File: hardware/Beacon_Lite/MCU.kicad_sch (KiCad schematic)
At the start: 11 parts, among them J2 0402, SW1 SW_Push, SW2 SW_Push, U1 ESP32-S3FH4R2

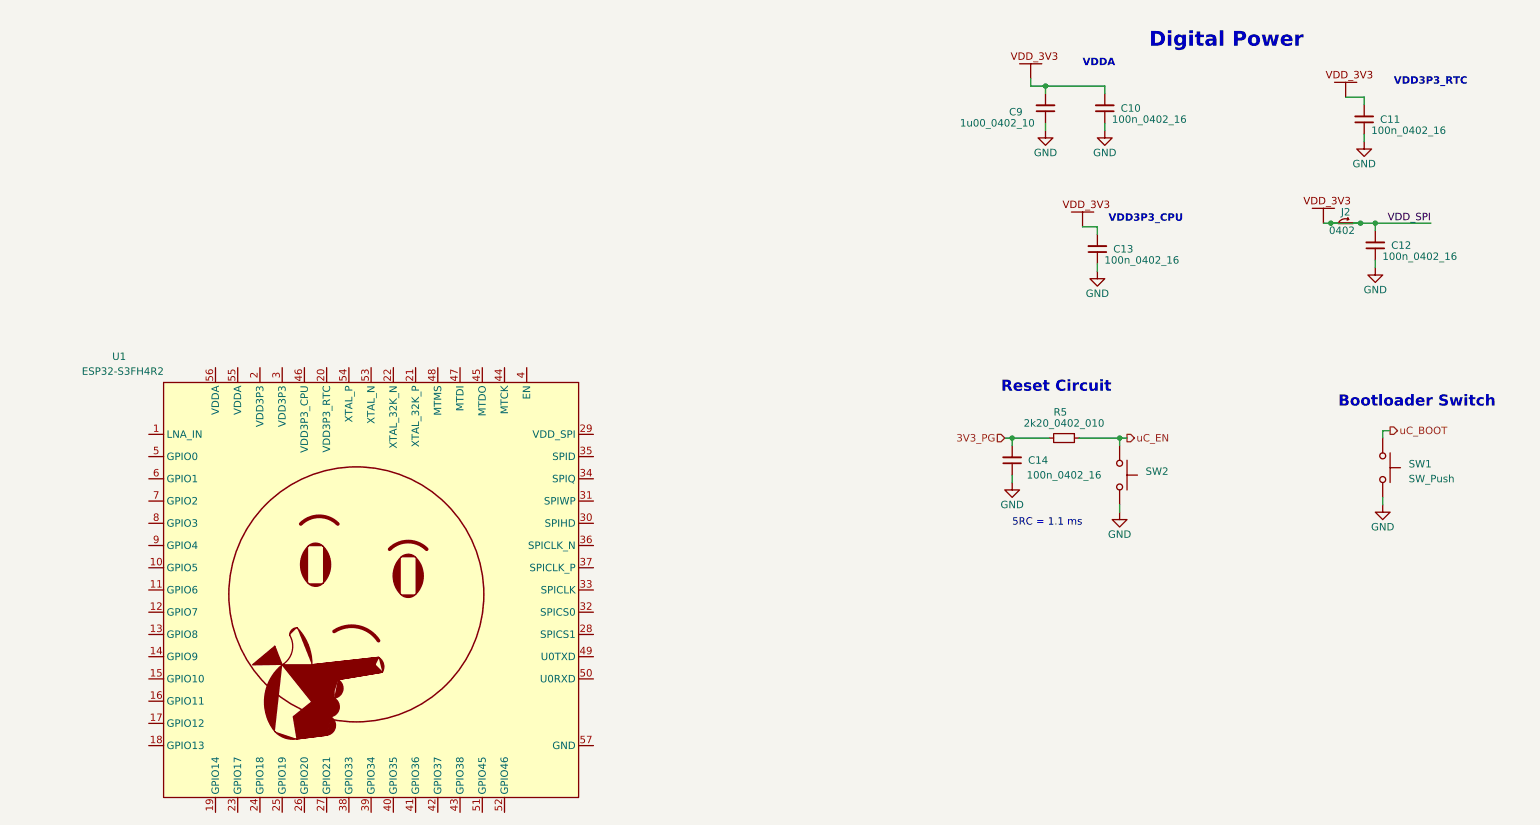
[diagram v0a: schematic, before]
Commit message: Started ST project. Create sch symbols.
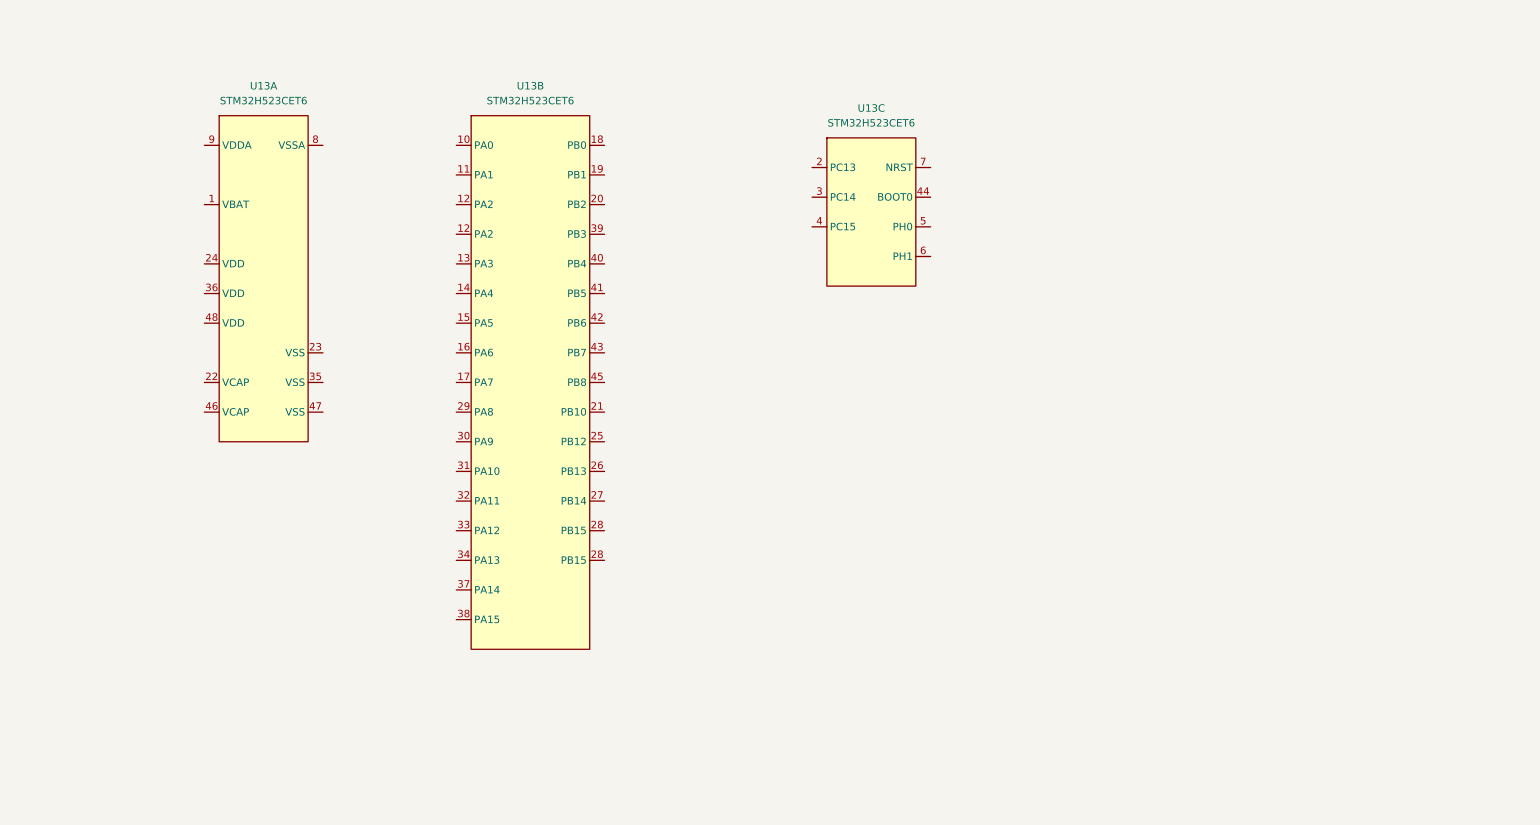
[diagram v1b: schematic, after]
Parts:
- removed C10, C11, C12, C13, C14: 100n_0402_16, Footprint_Library:0402_1005Metric_Handsolder, symbol Device:C_Small
- removed C9: 1u00_0402_10, Footprint_Library:0402_1005Metric_Handsolder, symbol Device:C_Small
- removed J2: 0402, Footprint_Library:0402_CUT-N-JUMP, symbol Beacon_Library:CUT_N_JUMP
- removed R5: 2k20_0402_010, Footprint_Library:0402_1005Metric_Handsolder, symbol Device:R_Small
- removed SW1, SW2: SW_Push, Footprint_Library:SW_PUSH_6mm, symbol Switch:SW_Push
- removed U1: ESP32-S3FH4R2, Footprint_Library:QFN40P700X700X90-57N-D, symbol Beacon_Library:ESP32-S3FH4R2
- added U13: STM32H523CET6, symbol Beacon_Lite_Library:STM32H523CET6
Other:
- note removed: "5RC = 1.1 ms"
- note removed: "Bootloader Switch"
- note removed: "Digital Power"
- note removed: "Reset Circuit"
- note removed: "VDD3P3_CPU"
- note removed: "VDD3P3_RTC"
- note removed: "VDDA"

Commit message: Minor schematic and symbol updates
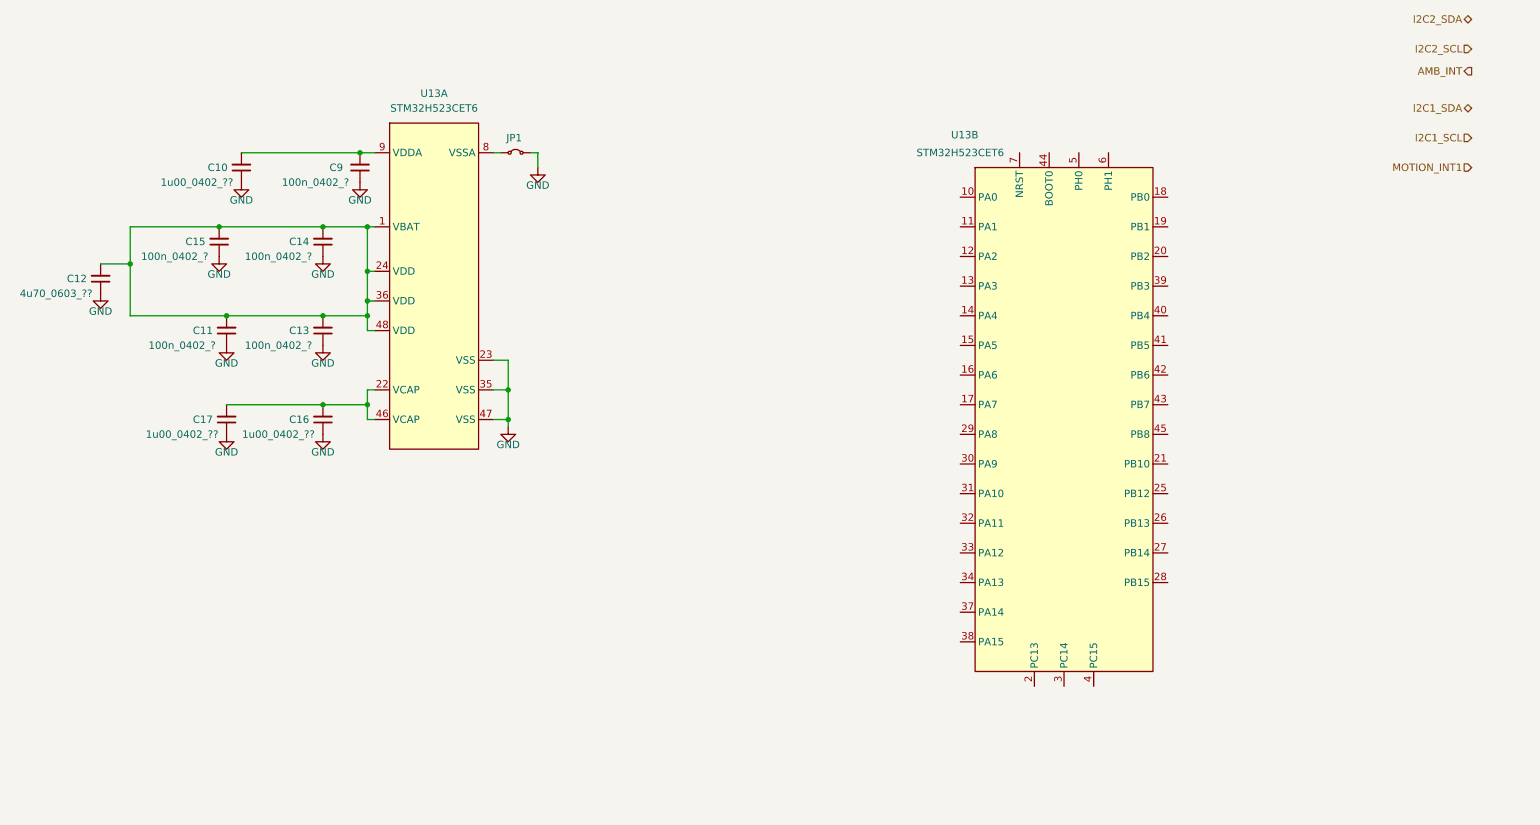
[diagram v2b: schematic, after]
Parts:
- removed unit 3 of U13
- added C10, C16, C17: 1u00_0402_??, Footprint_Library:0402_1005Metric_Handsolder, symbol Device:C_Small
- added C11, C13, C14, C15, C9: 100n_0402_?, Footprint_Library:0402_1005Metric_Handsolder, symbol Device:C_Small
- added C12: 4u70_0603_??, Footprint_Library:0402_1005Metric_Handsolder, symbol Device:C_Small
- added JP1: Jumper_2_Small_Bridged, symbol Jumper:Jumper_2_Small_Bridged
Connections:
- net at U13.1 (VBAT): now also U13.24 (VDD), U13.36 (VDD), U13.48 (VDD), C11.2, C12.2, C13.2, C14.2, C15.2
- net at U13.22 (VCAP): now also U13.46 (VCAP), C16.2, C17.2
- net GND: now reaches U13.23 (VSS)
- net GND: now also U13.35 (VSS), U13.47 (VSS), C10.1, C11.1, C12.1, C13.1, C14.1, C15.1, C16.1, C17.1, C9.1, JP1.2 (B)
- net at U13.8 (VSSA): now also JP1.1 (A)
- net at U13.9 (VDDA): now also C10.2, C9.2
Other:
- moved on the sheet: U13A
